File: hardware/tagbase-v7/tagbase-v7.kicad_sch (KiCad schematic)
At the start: 40 parts, among them J1 Conn_01x04_Female, J101 Conn_02x03_Odd_Even, J102 Conn_02x05_Odd_Even, J104 USB_B_Mini, J2 Conn_01x06, J5 Conn_01x02, SW1 SW_DIP_x04, U1 XC6206, U105 Tactile Switch, U2 TS5A3159ADBVR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

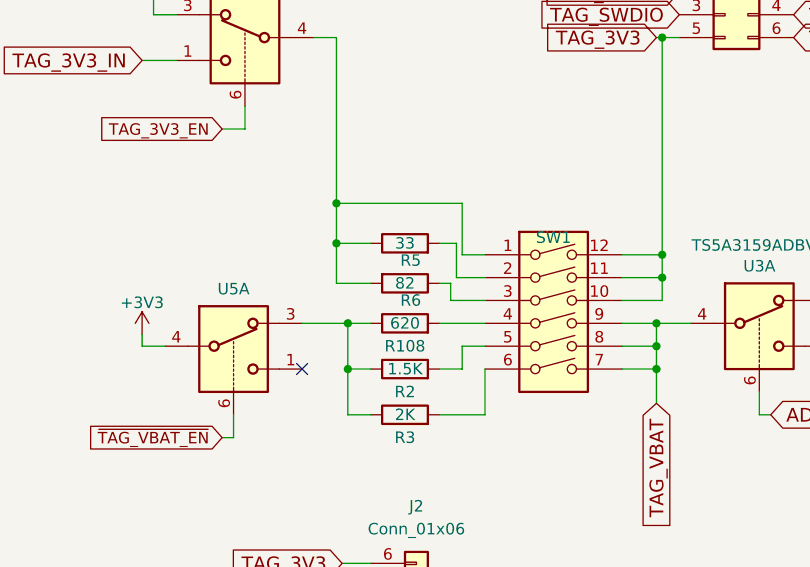
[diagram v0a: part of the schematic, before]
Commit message: fix tagbase v7 for jlcpcb fabrication
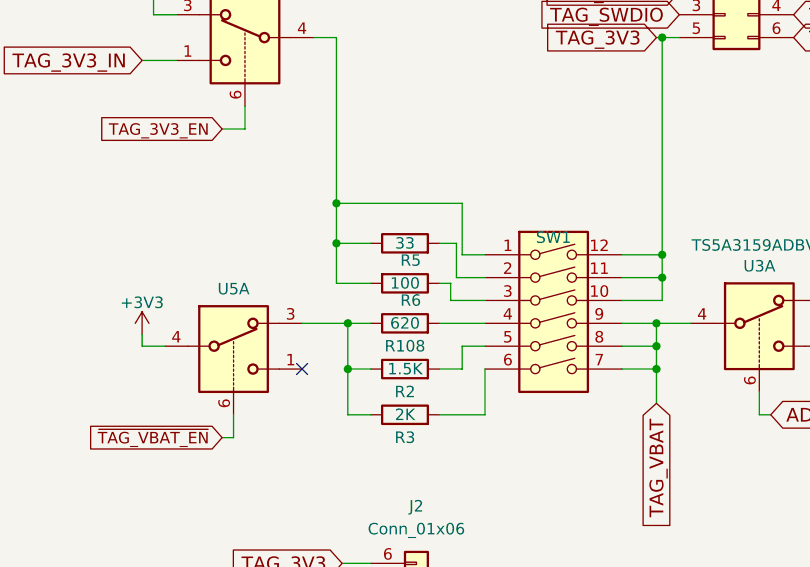
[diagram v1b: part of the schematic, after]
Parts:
- H1, H2, H3, H4, J1, J101, J102, J2, J5: now left out of the parts list
- J104, SW1, U6: JlcRotOffset (none) -> -90
- R6: value 82 -> 100; LCSC C23255 -> C22775; MPN 0603WAF820JT5E -> 0603WAF1000T5E
- U1, U2, U3, U4, U5: JlcRotOffset (none) -> 180
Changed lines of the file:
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@@
+      (effects (font (size 1.27 1.27)) hide)
+    )
+    (property "JlcRotOffset" "-90" (id 7) (at 57.15 170.18 0)
       (effects (font (size 1.27 1.27)) hide)
     )
@@
   )
   (symbol (lib_id "Connector_Generic:Conn_02x03_Odd_Even") (at 237.49 29.21 0) (unit 1)
-    (in_bom yes) (on_board yes)
+    (in_bom no) (on_board yes)
     (property "Reference" "J101" (id 0) (at 238.76 23.495 0))
     (property "Value" "Conn_02x03_Odd_Even" (id 1) (at 238.76 23.4696 0)
@@
   )
   (symbol (lib_id "Connector_Generic:Conn_02x05_Odd_Even") (at 102.87 172.72 0) (unit 1)
-    (in_bom yes) (on_board yes)
+    (in_bom no) (on_board yes)
     (property "Reference" "J102" (id 0) (at 104.14 164.465 0))
     (property "Value" "Conn_02x05_Odd_Even" (id 1) (at 104.14 164.4396 0)
@@
       (effects (font (size 1.27 1.27)) hide)
     )
+    (property "JlcRotOffset" "180" (id 7) (at 35.56 106.68 0)
+      (effects (font (size 1.27 1.27)) hide)
+    )
     (pin "1")
     (pin "3")
@@
       (effects (font (size 1.27 1.27)) hide)
     )
+    (property "JlcRotOffset" "180" (id 7) (at 220.98 130.81 0)
+      (effects (font (size 1.27 1.27)) hide)
+    )
     (pin "1")
     (pin "3")
@@
       (effects (font (size 1.27 1.27)) hide)
     )
+    (property "JlcRotOffset" "180" (id 7) (at 233.68 130.81 0)
+      (effects (font (size 1.27 1.27)) hide)
+    )
     (pin "1")
     (pin "3")
@@
     )
     (property "LCSC" "C128405" (id 6) (at 241.3 60.96 0)
+      (effects (font (size 1.27 1.27)) hide)
+    )
+    (property "JlcRotOffset" "180" (id 7) (at 241.3 60.96 0)
       (effects (font (size 1.27 1.27)) hide)
     )
@@
       (effects (font (size 1.27 1.27)) hide)
     )
+    (property "JlcRotOffset" "180" (id 7) (at 54.61 29.21 0)
+      (effects (font (size 1.27 1.27)) hide)
+    )
     (pin "1")
     (pin "2")
@@
     )
     (property "LCSC" "C3293146" (id 6) (at 218.44 63.5 0)
+      (effects (font (size 1.27 1.27)) hide)
+    )
+    (property "JlcRotOffset" "-90" (id 7) (at 218.44 63.5 0)
       (effects (font (size 1.27 1.27)) hide)
     )
@@
   )
   (symbol (lib_id "Connector_Generic:Conn_01x04") (at 238.76 96.52 0) (unit 1)
-    (in_bom yes) (on_board yes)
+    (in_bom no) (on_board yes)
     (property "Reference" "J1" (id 0) (at 239.4458 97.1296 0)
       (effects (font (size 1.27 1.27)) (justify left))
@@
     )
     (property "LCSC" "C128405" (id 6) (at 184.15 29.21 0)
+      (effects (font (size 1.27 1.27)) hide)
+    )
+    (property "JlcRotOffset" "180" (id 7) (at 184.15 29.21 0)
       (effects (font (size 1.27 1.27)) hide)
     )
@@
       (effects (font (size 1.27 1.27)) hide)
     )
+    (property "JlcRotOffset" "180" (id 7) (at 209.55 130.81 0)
+      (effects (font (size 1.27 1.27)) hide)
+    )
     (pin "1")
     (pin "3")
@@
       (effects (font (size 1.27 1.27)) hide)
     )
+    (property "JlcRotOffset" "180" (id 7) (at 182.88 63.5 0)
+      (effects (font (size 1.27 1.27)) hide)
+    )
     (pin "1")
     (pin "3")
@@
       (effects (font (size 1.27 1.27)) hide)
     )
+    (property "JlcRotOffset" "180" (id 7) (at 247.65 130.81 0)
+      (effects (font (size 1.27 1.27)) hide)
+    )
     (pin "1")
     (pin "3")
@@
   )
   (symbol (lib_id "Connector_Generic:Conn_01x02") (at 30.48 127 180) (unit 1)
-    (in_bom yes) (on_board yes)
+    (in_bom no) (on_board yes)
     (property "Reference" "J5" (id 0) (at 32.5628 121.0818 0))
     (property "Value" "Conn_01x02" (id 1) (at 32.5628 121.0564 0)
@@
   )
   (symbol (lib_id "Mechanical:MountingHole") (at 171.45 133.35 0) (unit 1)
-    (in_bom yes) (on_board yes) (fields_autoplaced)
+    (in_bom no) (on_board yes) (fields_autoplaced)
     (property "Reference" "H3" (id 0) (at 173.99 133.3499 0)
       (effects (font (size 1.27 1.27)) (justify left))
@@
   )
   (symbol (lib_id "Connector_Generic:Conn_01x06") (at 203.2 97.79 0) (mirror x) (unit 1)
-    (in_bom yes) (on_board yes) (fields_autoplaced)
+    (in_bom no) (on_board yes) (fields_autoplaced)
     (property "Reference" "J2" (id 0) (at 203.2 83.82 0))
     (property "Value" "Conn_01x06" (id 1) (at 203.2 86.36 0))
@@
     (in_bom yes) (on_board yes)
     (property "Reference" "R6" (id 0) (at 202.565 60.96 90))
-    (property "Value" "82" (id 1) (at 201.93 59.055 90))
+    (property "Value" "100" (id 1) (at 201.93 59.055 90))
     (property "Footprint" "Resistor_SMD:R_0603_1608Metric" (id 2) (at 201.93 57.277 90)
       (effects (font (size 1.27 1.27)) hide)
@@
       (effects (font (size 1.27 1.27)) hide)
     )
-    (property "MPN" "0603WAF820JT5E" (id 5) (at 201.93 59.055 90)
-      (effects (font (size 1.27 1.27)) hide)
-    )
-    (property "LCSC" "C23255" (id 6) (at 201.93 59.055 90)
+    (property "MPN" "0603WAF1000T5E" (id 5) (at 201.93 59.055 90)
+      (effects (font (size 1.27 1.27)) hide)
+    )
+    (property "LCSC" "C22775 " (id 6) (at 201.93 59.055 90)
       (effects (font (size 1.27 1.27)) hide)
     )
@@
   )
   (symbol (lib_id "Mechanical:MountingHole") (at 171.45 128.905 0) (unit 1)
-    (in_bom yes) (on_board yes) (fields_autoplaced)
+    (in_bom no) (on_board yes) (fields_autoplaced)
     (property "Reference" "H2" (id 0) (at 173.99 128.9049 0)
       (effects (font (size 1.27 1.27)) (justify left))
@@
   )
   (symbol (lib_id "Mechanical:MountingHole") (at 171.45 124.46 0) (unit 1)
-    (in_bom yes) (on_board yes) (fields_autoplaced)
+    (in_bom no) (on_board yes) (fields_autoplaced)
     (property "Reference" "H1" (id 0) (at 173.99 124.4599 0)
       (effects (font (size 1.27 1.27)) (justify left))
@@
     )
     (property "LCSC" "C961597" (id 6) (at 92.71 90.17 0)
+      (effects (font (size 1.27 1.27)) hide)
+    )
+    (property "JlcRotOffset" "-90" (id 7) (at 92.71 90.17 0)
       (effects (font (size 1.27 1.27)) hide)
     )
@@
   )
   (symbol (lib_id "Mechanical:MountingHole") (at 171.45 137.795 0) (unit 1)
-    (in_bom yes) (on_board yes) (fields_autoplaced)
+    (in_bom no) (on_board yes) (fields_autoplaced)
     (property "Reference" "H4" (id 0) (at 173.99 137.7949 0)
       (effects (font (size 1.27 1.27)) (justify left))
@@
     )
     (path "/47ee72fe-3318-409a-ab4e-3ed3b6624673"
-      (reference "R6") (unit 1) (value "82") (footprint "Resistor_SMD:R_0603_1608Metric")
+      (reference "R6") (unit 1) (value "100") (footprint "Resistor_SMD:R_0603_1608Metric")
     )
     (path "/00000000-0000-0000-0000-00005b038aed"
